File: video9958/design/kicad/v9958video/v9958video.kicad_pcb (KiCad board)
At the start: 4 copper layers, 106 x 89 mm, 59 parts, among them IC1 ATF16V8BQL-15, IC2 ATF16V8BQL-15, IC3 V9958, J1 Conn_02x32_Odd_Even, J2 Conn_02x06_Counter_Clockwise, J3 DIN-6, Q1 21.477MHz, Q2 2N3904, Q3 2N3906, Q4 2N3906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

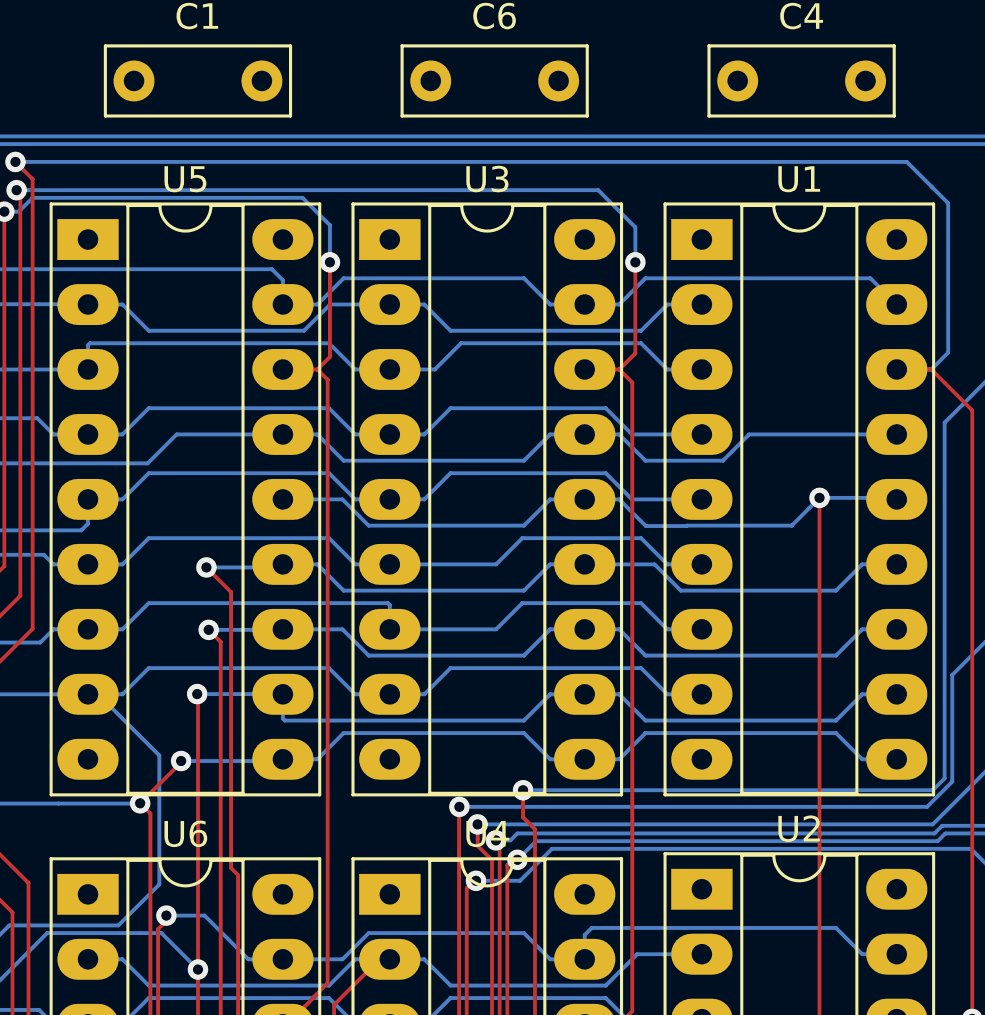
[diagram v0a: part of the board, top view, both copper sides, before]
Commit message: Make IC numbering less nonsensical
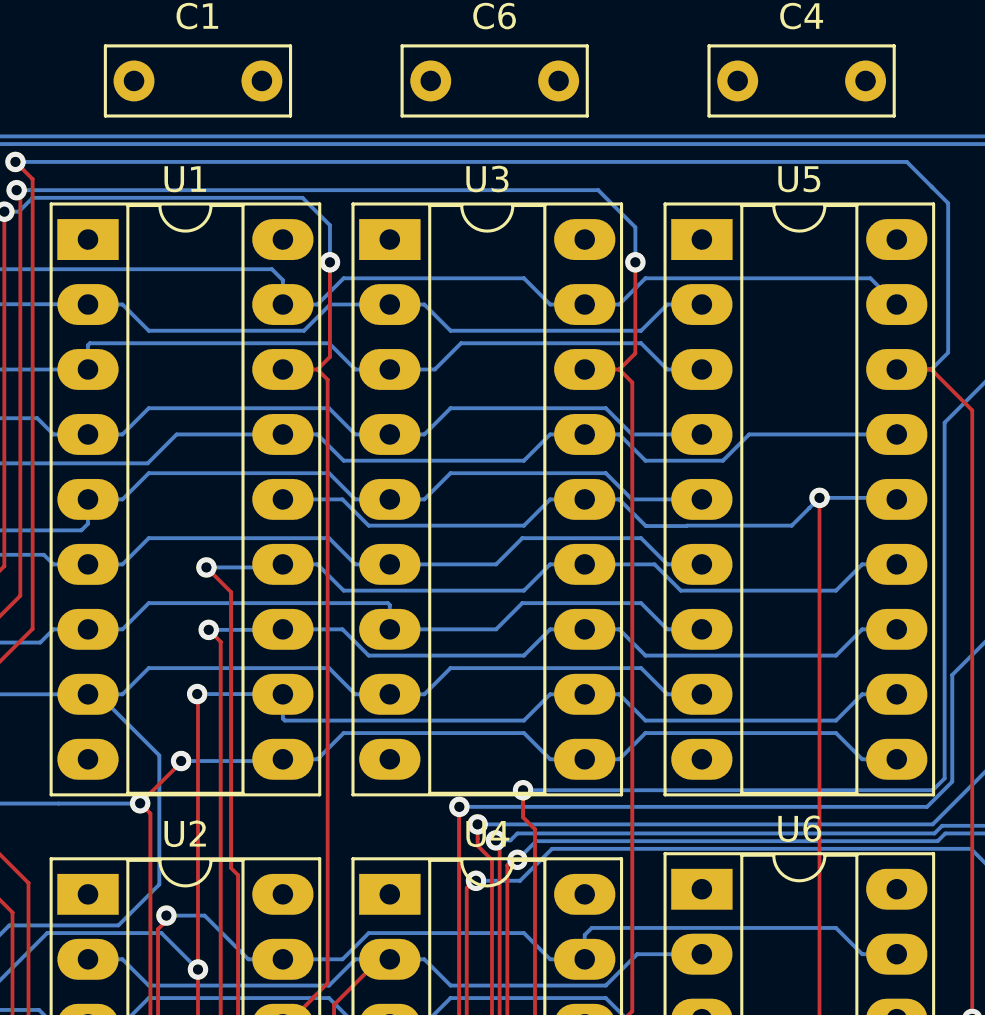
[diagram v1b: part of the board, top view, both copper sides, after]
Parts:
- renumbered U5 to U1, U6 to U2, U1 to U5, U2 to U6

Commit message: Revision 1.1 RTM
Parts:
- added C26: 100nF, Capacitor_THT:C_Rect_L7.0mm_W2.5mm_P5.00mm, F.Cu at (114.0, 67.0)
- added C27: 100nF, Capacitor_THT:C_Rect_L7.0mm_W2.5mm_P5.00mm, F.Cu at (138.8, 83.8)
- added C28: 100nF, Capacitor_THT:C_Rect_L7.0mm_W2.5mm_P5.00mm, F.Cu at (137.8, 49.8)
- C15: value 100uF -> 220uF; footprint Capacitor_THT:CP_Radial_D5.0mm_P2.50mm -> Capacitor_THT:CP_Radial_D6.3mm_P2.50mm
- moved C24 28.7 mm to (114.0, 96.0)
- moved C25 11.9 mm to (114.0, 85.0)
- moved R1 1.68 mm to (140.2, 38.2)
- moved R15 1.23 mm to (135.8, 84.1)
- moved R13 1.23 mm to (121.9, 84.2)
- moved R7 1.23 mm to (127.5, 84.2)
- moved R14 1.23 mm to (133.0, 84.1)
- moved R4 1.23 mm to (124.7, 84.2)
- moved R5 1.23 mm to (119.2, 84.2)
- moved R8 1.23 mm to (130.2, 84.1)
- moved C12 0.25 mm to (149.0, 35.2)
- moved C13 0.25 mm to (149.0, 40.0)
- moved Q1 0.25 mm to (157.2, 37.5)
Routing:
- net Net-(Q2-Pad2): track 53.2 -> 29.8 mm
- net Net-(C21-Pad2): track 37.8 -> 30.5 mm
- net /v9958-output/CSYNC: track 83.3 -> 76.5 mm
- net Net-(C16-Pad1): track 42.8 -> 39.6 mm, vias 0 -> 1
- net /v9958-output/BLUE: track 91.1 -> 88.2 mm, vias 2 -> 1
- net Net-(C19-Pad1): track 40.8 -> 37.9 mm
- net Net-(C22-Pad2): track 32.2 -> 33.9 mm
- net Net-(C17-Pad1): track 28.7 -> 30.0 mm
- net /v9958-output/GREEN: track 79.4 -> 80.7 mm, vias 2 -> 1
- net Net-(C20-Pad2): track 21.1 -> 22.3 mm
- net /v9958-output/RED: track 82.7 -> 83.5 mm
- net Net-(IC3-Pad3): track 8.88 -> 9.49 mm
- net VCC: track 12.0 -> 11.5 mm
- net OCSYNC: vias 1 -> 0
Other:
- board text added: "Revision 1.1 (June 2020)"
- board text removed: "Revision 1 (June 2020)"

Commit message: Final tweaks
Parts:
- moved U6 0.20 mm to (189.6, 65.8)
- renumbered IC3 to IC1, IC1 to IC2, IC2 to IC3
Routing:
- net VA0: track 90.7 -> 88.9 mm
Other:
- board text added: "Bigor"
- board text added: "EXT Video RAM"
- board text added: "Glue Logic"
- board text added: "RGB Out"
- board text added: "VRAM Bank 1"
- board text added: "VRAM Bank 2"
- board text added: "Yamaha V9958 VDP"

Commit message: VDP r1.2
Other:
- board text added: "1"
- board text added: "12"
- board text added: "2"
- board text added: "Revision 1.2 (August 2020)"
- board text removed: "Revision 1.1 (June 2020)"
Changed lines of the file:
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@@
   (general
     (thickness 1.6)
-    (drawings 25)
+    (drawings 30)
     (tracks 1280)
     (zones 0)
@@
     )
   )
+  (gr_line (start 130.95 109.75) (end 136 109.75) (layer F.SilkS) (width 0.12))
+  (gr_line (start 130.95 112.3) (end 130.95 109.75) (layer F.SilkS) (width 0.12))
+  (gr_text 12 (at 134.7 105.573809 90) (layer F.SilkS)
+    (effects (font (size 1 1) (thickness 0.15)))
+  )
+  (gr_text 2 (at 121.95 106.05 90) (layer F.SilkS)
+    (effects (font (size 1 1) (thickness 0.15)))
+  )
+  (gr_text 1 (at 122 113.25 90) (layer F.SilkS)
+    (effects (font (size 1 1) (thickness 0.15)))
+  )
   (gr_text "RGB Out  " (at 113.5 40.25 90) (layer F.SilkS)
     (effects (font (size 1.5 1.5) (thickness 0.3)))
@@
   (gr_line (start 112 30) (end 117 30) (layer Edge.Cuts) (width 0.05))
   (gr_line (start 112 119) (end 117 119) (layer Edge.Cuts) (width 0.05))
-  (gr_text "Revision 1.1 (June 2020)" (at 135.51 114.45 180) (layer F.SilkS)
+  (gr_text "Revision 1.2 (August 2020)" (at 135.51 114.45 180) (layer F.SilkS)
     (effects (font (size 1 1) (thickness 0.15)))
   )
@@
   (segment (start 131.75 86.75) (end 131.75 90.41808) (width 0.4) (layer B.Cu) (net 115))
   (segment (start 133.00192 91.67) (end 135.767304 91.67) (width 0.4) (layer B.Cu) (net 115))
-  (segment (start 140.25 43.33) (end 140.25 50.9704) (width 0.15) (layer F.Cu) (net 124))
-  (segment (start 140.8496 51.57) (end 140.25 50.9704) (width 0.15) (layer F.Cu) (net 124))
-  (segment (start 141.8496 51.57) (end 140.8496 51.57) (width 0.15) (layer F.Cu) (net 124))
   (segment (start 117.38 59.13) (end 115 56.75) (width 0.4) (layer F.Cu) (net 116))
   (segment (start 117.38 64.8) (end 117.38 59.13) (width 0.4) (layer F.Cu) (net 116))
@@
   (segment (start 118.5 76.398946) (end 117.25 77.648946) (width 0.4) (layer B.Cu) (net 117))
   (segment (start 118.5 72.975) (end 118.5 76.398946) (width 0.4) (layer B.Cu) (net 117))
+  (segment (start 140.25 43.33) (end 140.25 50.9704) (width 0.15) (layer F.Cu) (net 124))
+  (segment (start 140.8496 51.57) (end 140.25 50.9704) (width 0.15) (layer F.Cu) (net 124))
+  (segment (start 141.8496 51.57) (end 140.8496 51.57) (width 0.15) (layer F.Cu) (net 124))
   (zone (net 1) (net_name GND) (layer In1.Cu) (hatch edge 0.508)
     (connect_pads (clearance 0.508))

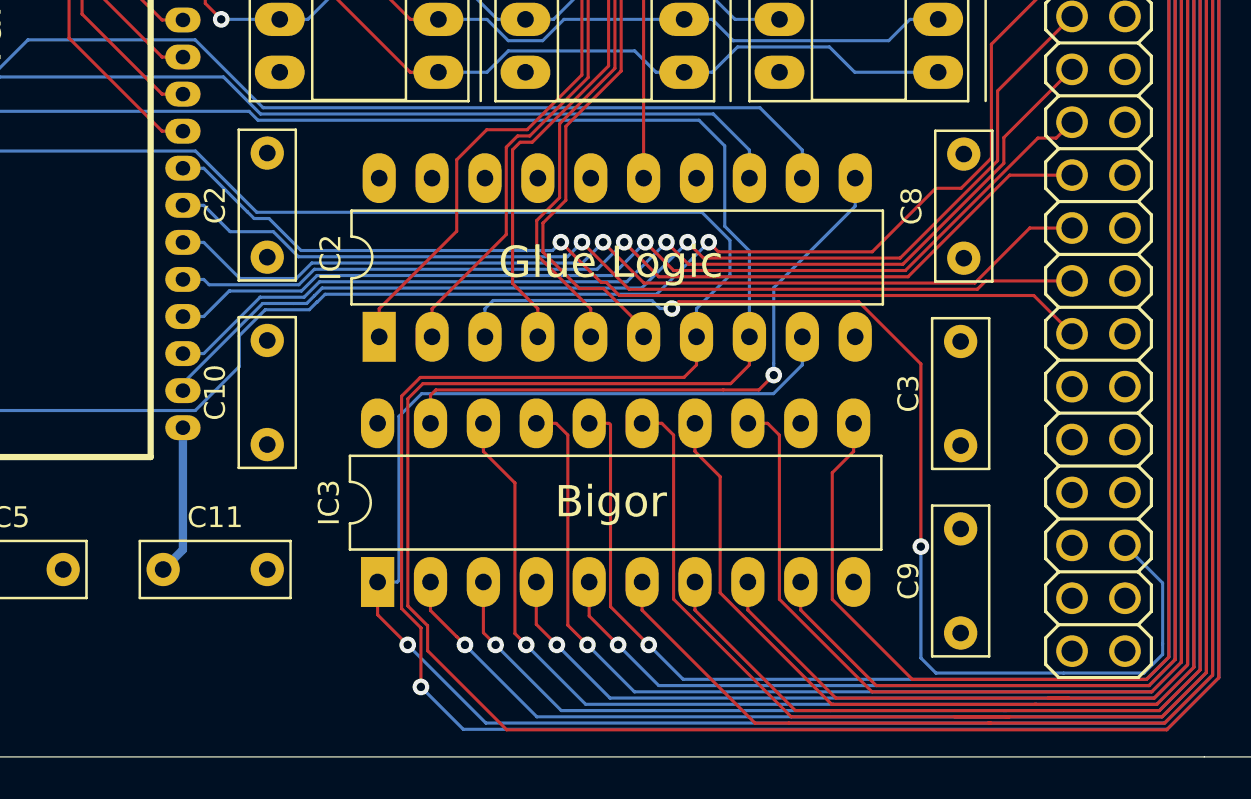
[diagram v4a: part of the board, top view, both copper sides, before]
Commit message: Add jumper to support 1.2 mainboard
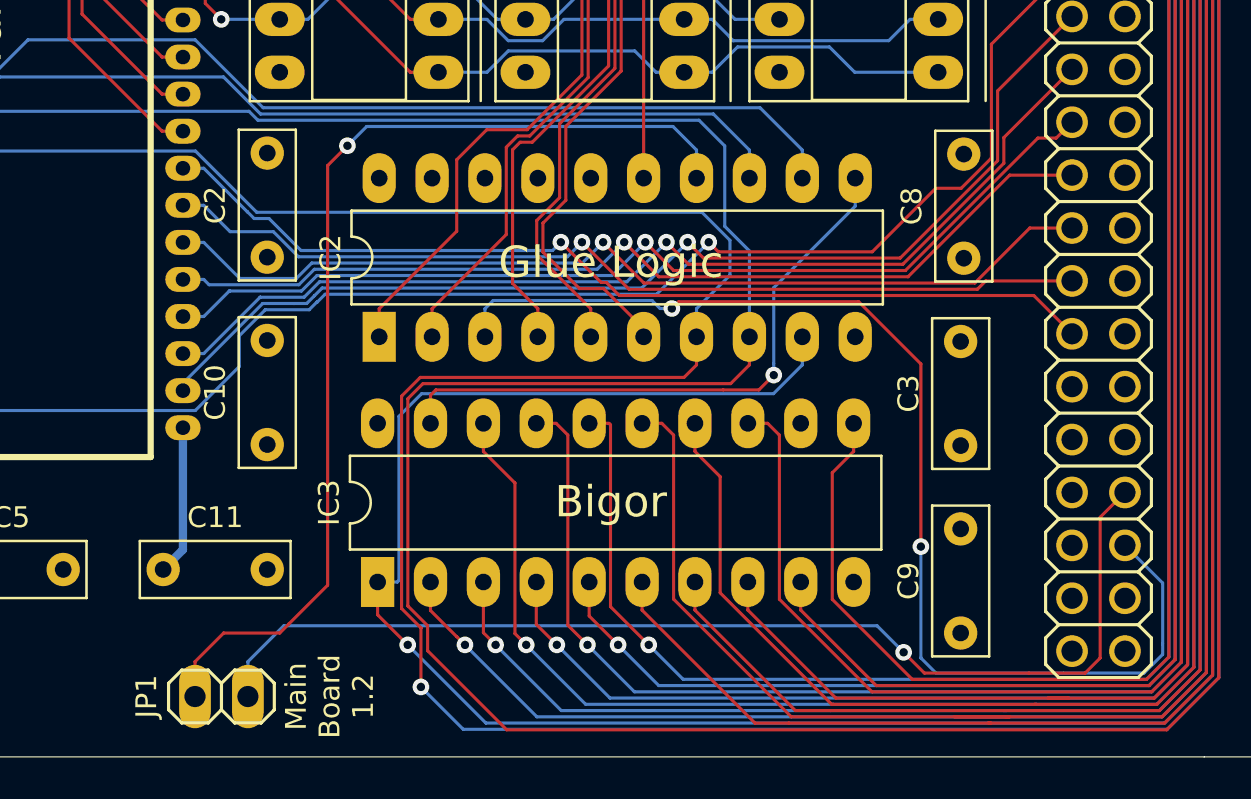
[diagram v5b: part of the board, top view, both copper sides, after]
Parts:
- added JP1: Jumper, rosco_m68k:pin-1X02, F.Cu at (162.8, 116.1)
- moved REF** 0.62 mm to (130.0, 115.6)
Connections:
- IC2 pad 14: Net-(IC2-Pad14) -> VDTACK
- J1 pad 58: Net-(J1-Pad58) -> DTACK
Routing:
- net DTACK: track 0.00 -> 53.0 mm, vias 0 -> 1
- net VDTACK: track 0.00 -> 50.0 mm, vias 0 -> 1
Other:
- board text added: "Main Board 1.2"
